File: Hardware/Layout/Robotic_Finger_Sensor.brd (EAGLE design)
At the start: 14 x 15.2 mm, 18 parts, among them U1 VCNL4040, U3 MS5637

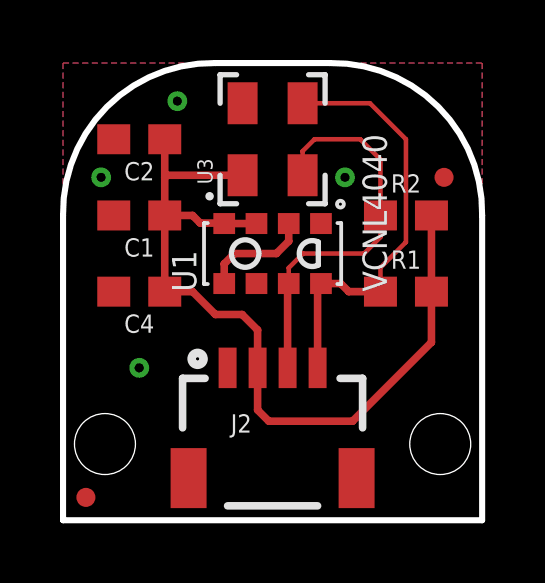
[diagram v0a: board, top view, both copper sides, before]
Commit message: Update to LPS25HB pressure sensor
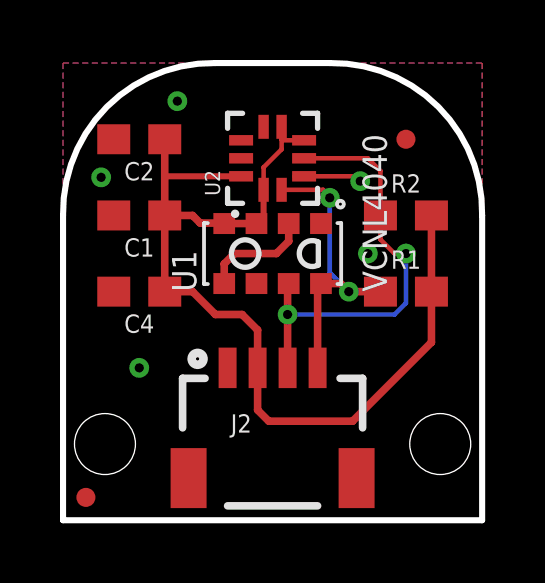
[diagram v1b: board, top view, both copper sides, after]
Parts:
- removed U$10: (no value), buzzard_labels:SENSOR5
- removed U$5: (no value), buzzard_labels:ROBOTIC3
- removed U$8: (no value), buzzard_labels:FINGER4
- removed U3: MS5637, MS5637:MS5637
- added U$6: (no value), buzzard_labels:ROBOTIC0
- added U$7: (no value), buzzard_labels:SENSOR2
- added U$9: (no value), buzzard_labels (1):FINGER0
- added U2: LPS25HB, LPS25HB:LPS25HB
- C1: value 2.2uF -> 4.7uF
- moved FD1 1.80 mm to (11.4, 12.7)
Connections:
- removed net SCL: J2.4, R1.1, U1.8, U3.3
- removed net SDA: J2.3, R2.1, U1.7, U3.2
- new net SCL/SCK: J2.4, R1.1, U1.8, U2.2
- new net SDA/MOSI: J2.3, R2.1, U1.7, U2.4
- net 3.3V: now also U2.1, U2.10, U2.5, U2.6; no longer U3.1
- net GND: now also U2.3, U2.8, U2.9; no longer U3.4
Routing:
- net SDA/MOSI: track 0.00 -> 14.6 mm, vias 0 -> 2
- net SCL: track 14.3 -> 0.00 mm
- net SDA: track 13.3 -> 0.00 mm
- net SCL/SCK: track 0.00 -> 10.1 mm, vias 0 -> 2
- net 3.3V: track 29.4 -> 33.7 mm
- net GND: track 0.00 -> 2.26 mm, vias 4 -> 5
